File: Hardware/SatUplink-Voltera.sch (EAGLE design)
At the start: 40 parts, among them U1 MIC5219-3.3, U2 AP7311-1.8, U3 74HC4050, U4 SPOT-CONNECT, U5 ARDUINO_SHIELD, U6 MIC5219-3.0, U7 MIC5219-3.0

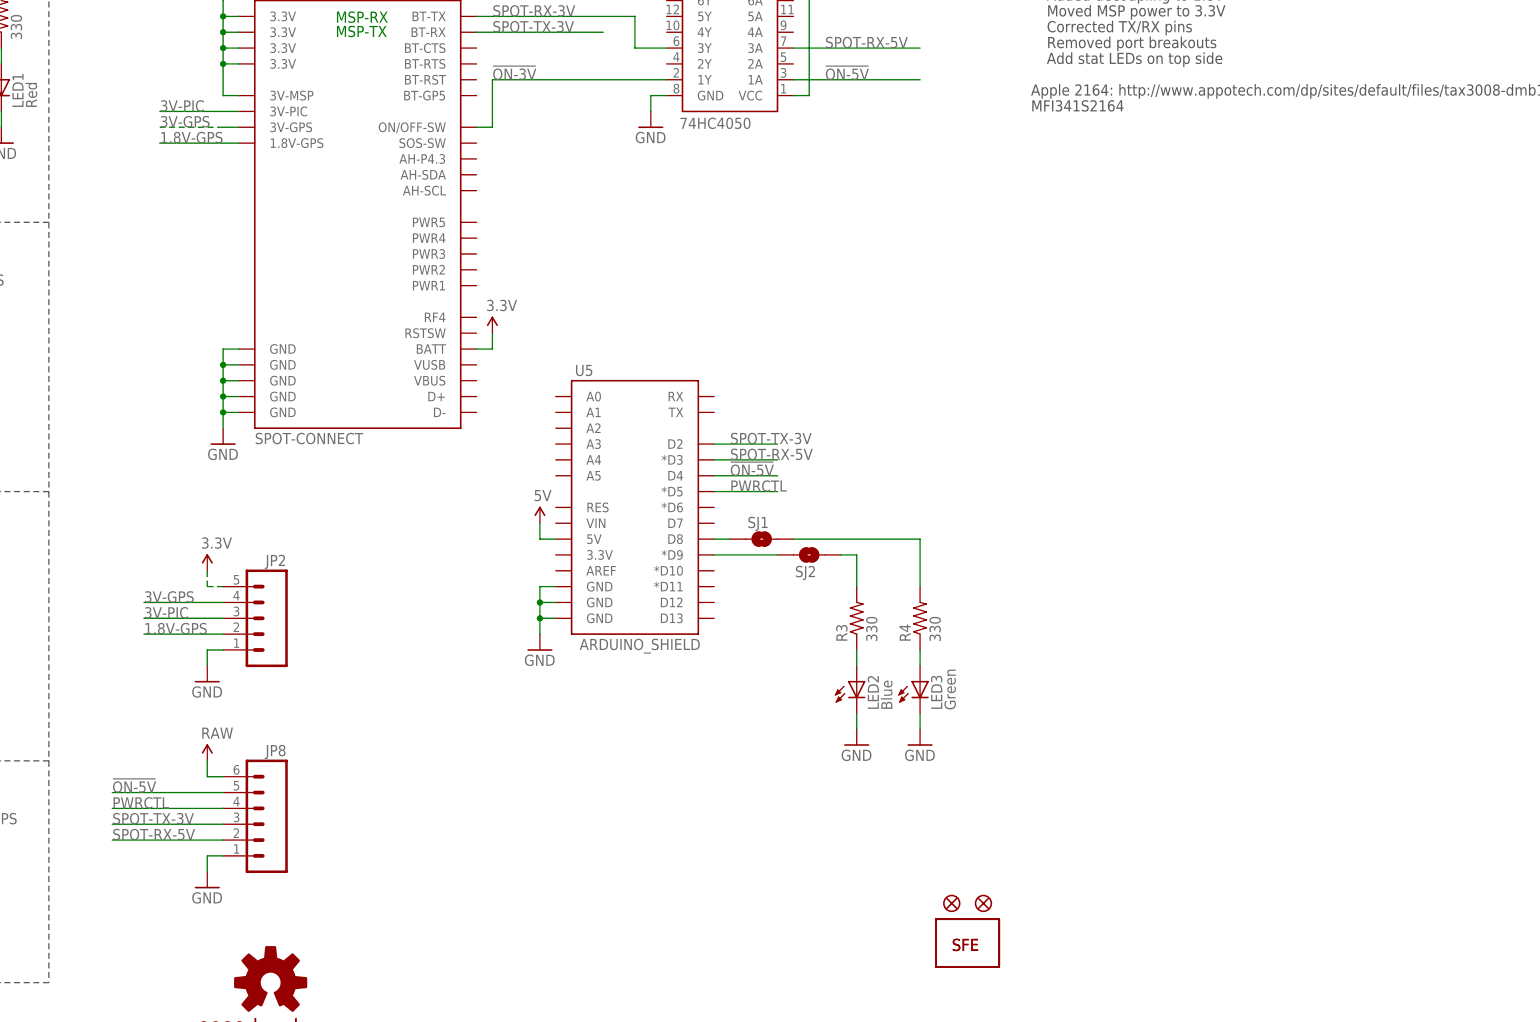
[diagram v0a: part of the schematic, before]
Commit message: Voltera Edits
The V12 board has been edited to fit onto the Voltera Arduino Uno
substrate board.
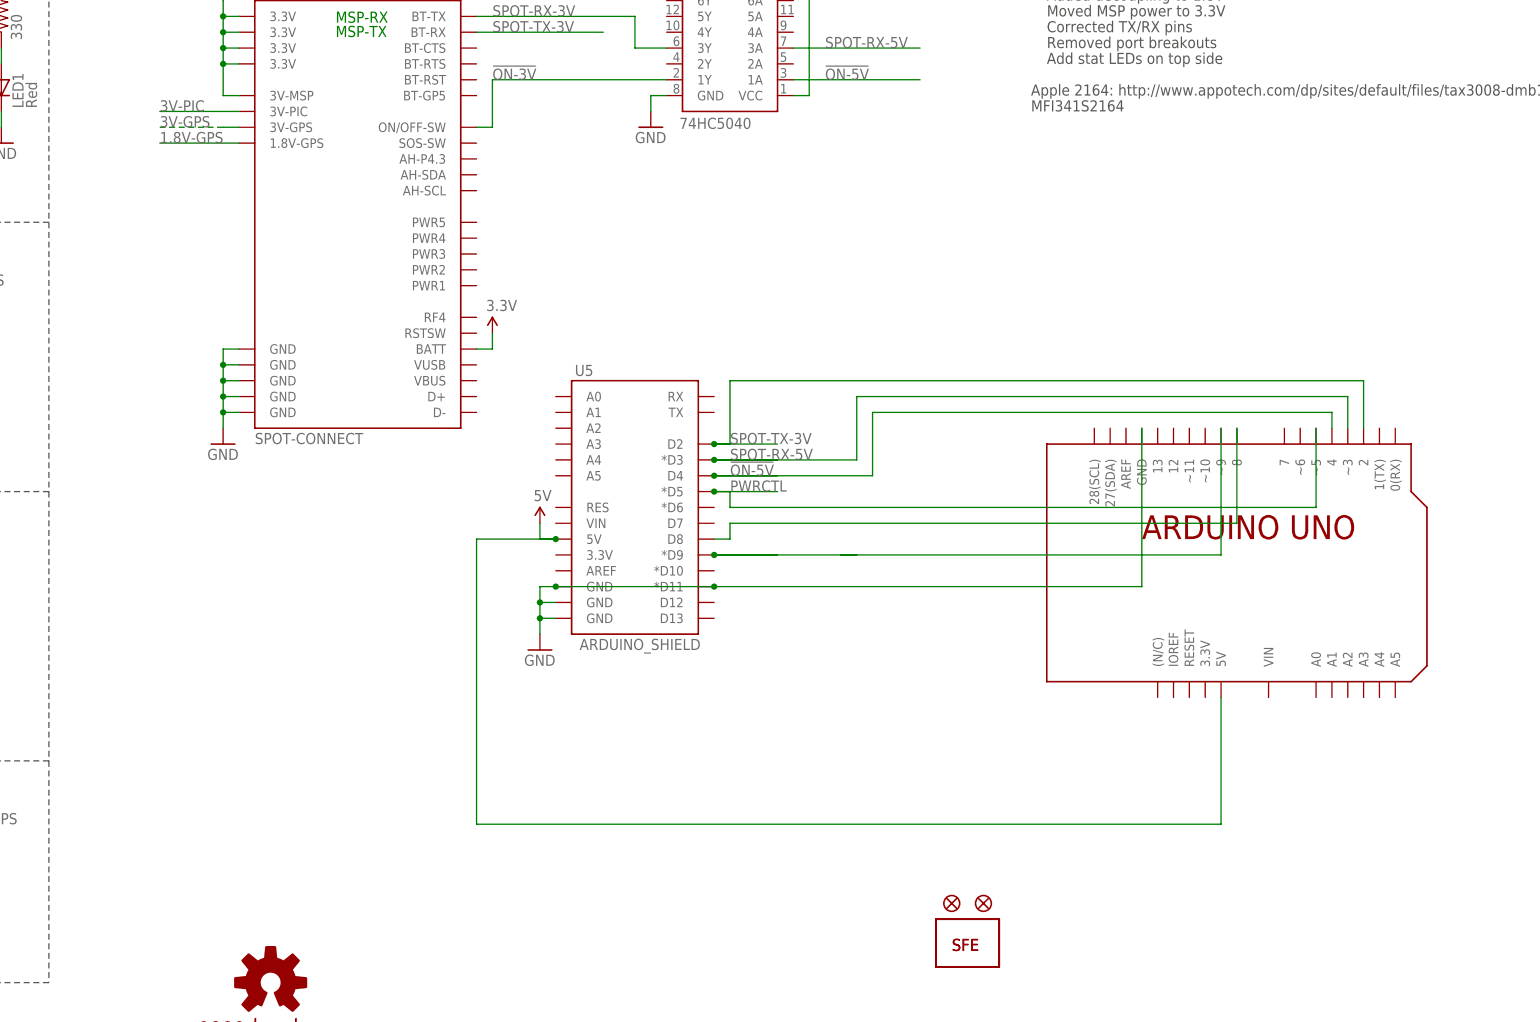
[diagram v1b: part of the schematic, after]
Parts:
- removed JP2: (no value), SparkFun:M05PTH
- removed JP8: (no value), SparkFun:M06SIP
- removed LED2: Blue, SparkFun:LED0603
- removed LED3: Green, SparkFun:LED0603
- removed R3, R4: 330, SparkFun:RESISTOR0402-RES
- removed SJ1, SJ2: SOLDERJUMPERTRACE, SparkFun:SOLDERJUMPERTRACE
- added U$4: TEMPLATE_ARDUINO_UNO_SHIELD, voltera_EAGLE_community_lib:TEMPLATE_ARDUINO_UNO_SHIELD
- U3: value 74HC4050 -> 74HC5040
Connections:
- removed net N$2: R4.2, SJ1.2
- removed net N$3: R3.2, SJ2.2
- removed net N$5: LED2.A, R3.1
- removed net N$6: LED3.A, R4.1
- net !ON-5V: now also U$4.4; no longer JP8.5
- net 1.8V-GPS: no longer JP2.2
- net 3.3V: no longer JP2.5
- net 3V-GPS: no longer JP2.4
- net 3V-PIC: no longer JP2.3
- net 5V: now also U$4.5V; no longer JP8.6
- net GND: now also U$4.GND, U5.*D11; no longer JP2.1, JP8.1, LED2.C, LED3.C
- net N$7: now also U$4.8; no longer SJ1.1
- net N$8: now also U$4.~9; no longer SJ2.1
- net PWRCTL: now also U$4.~5; no longer JP8.4
- net SPOT-RX-5V: now also U$4.~3; no longer JP8.2
- net SPOT-TX-3V: now also U$4.2; no longer JP8.3
